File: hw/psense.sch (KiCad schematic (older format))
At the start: 8 parts

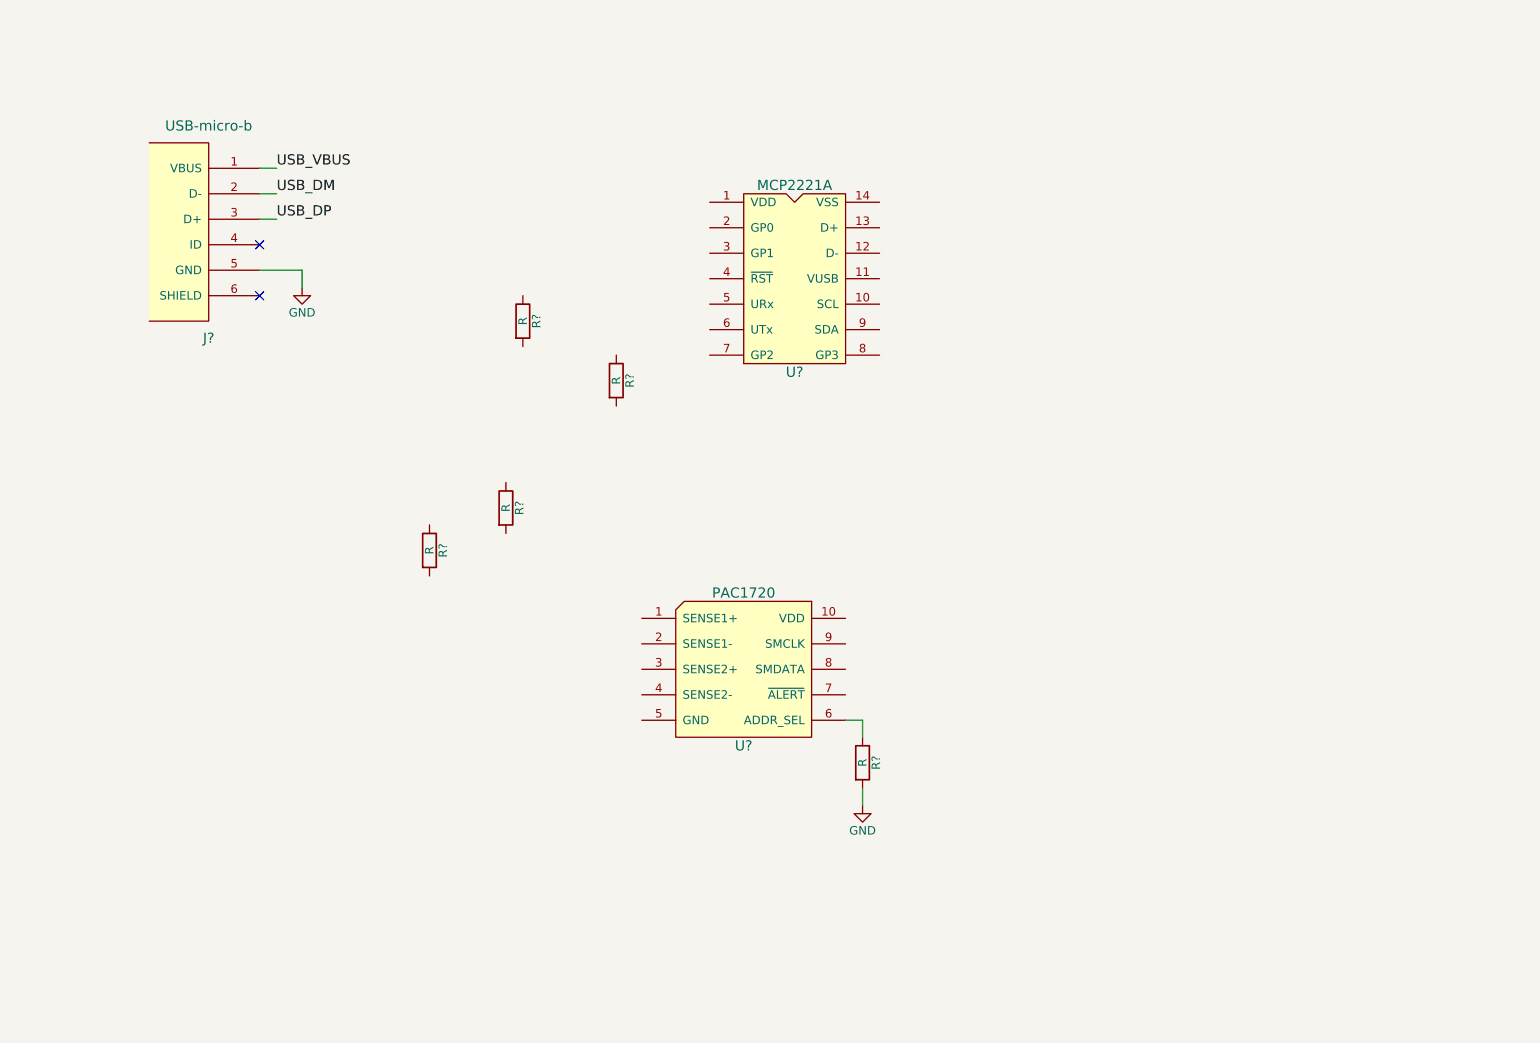
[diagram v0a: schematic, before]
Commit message: Most of schematic done
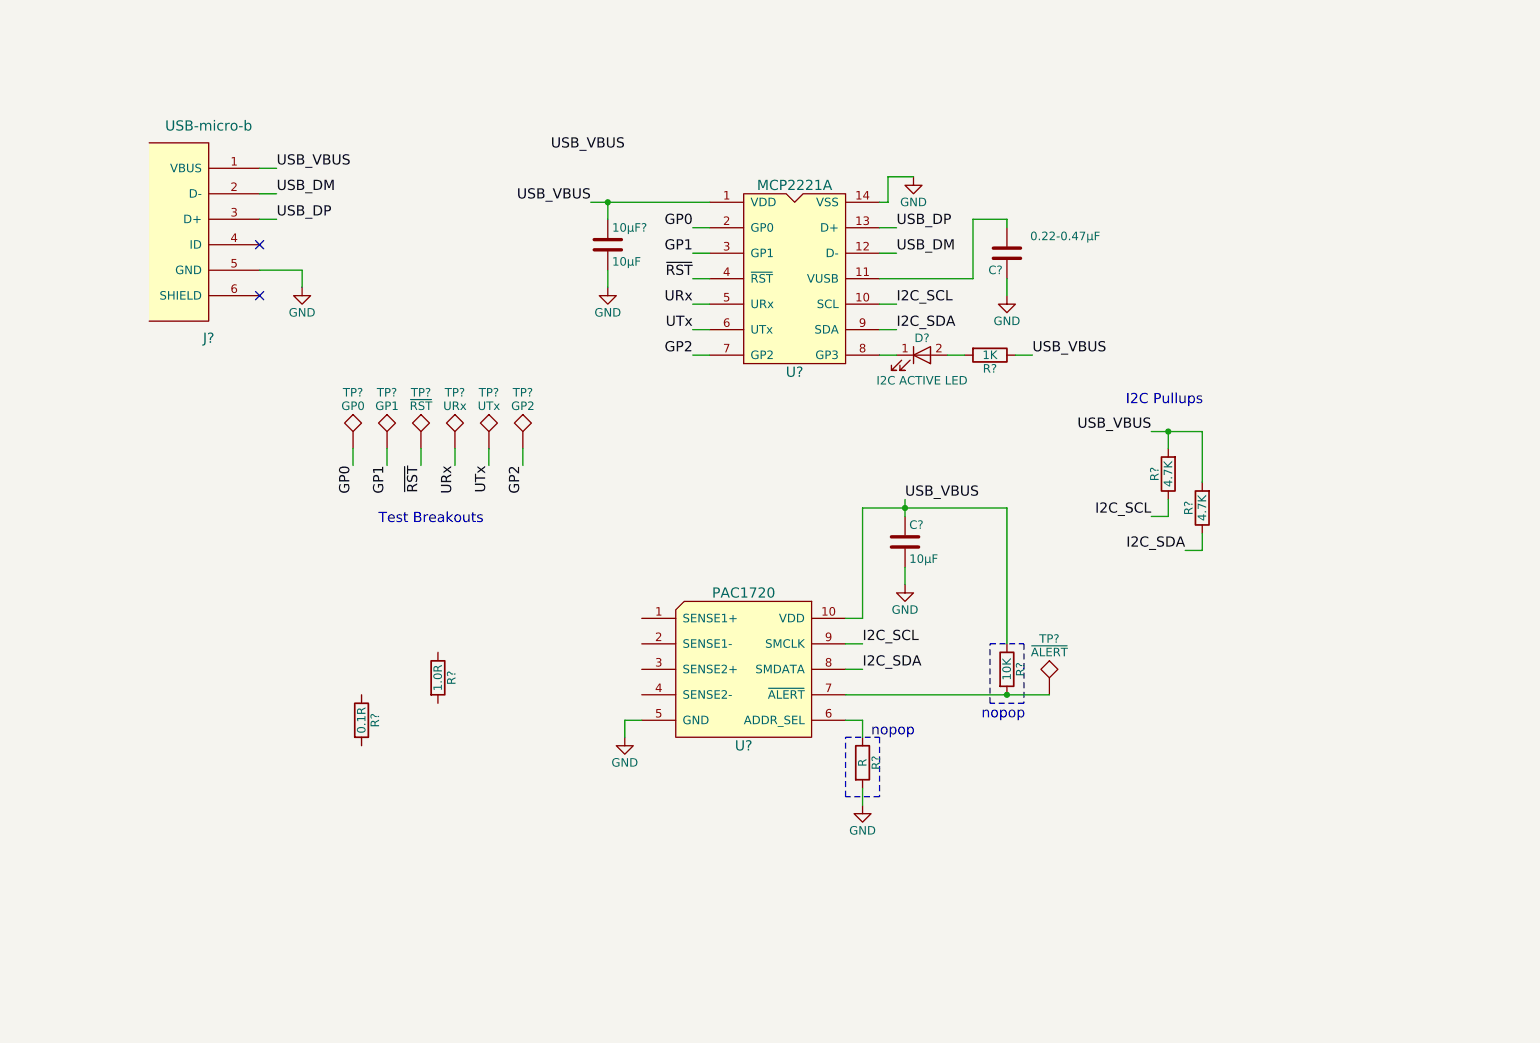
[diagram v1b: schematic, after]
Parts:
- removed R? (x2): R, symbol R
- added 10µF?, C?: 10µF, symbol C
- added C?: 0.22-0.47µF, symbol C
- added D?: I2C ACTIVE LED, symbol LED
- added R?: 10K, symbol R
- added R?: 1K, symbol R
- added R? (x2): 4.7K, symbol R
- added TP?: ~ALERT, symbol TEST
- added TP?: GP2, symbol TEST
- added TP?: URx, symbol TEST
- added TP?: UTx, symbol TEST
- added TP?: ~RST, symbol TEST
- added TP?: GP1, symbol TEST
- added TP?: GP0, symbol TEST
- R?: value R -> 0.1R
- R?: value R -> 1.0R
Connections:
- net GND: now also U?.14 (VSS), U?.5 (GND), 10µF?.2, C?.1, C?.2
- net USB_DM: now also U?.12 (D-)
- net USB_DP: now also U?.13 (D+)
- net USB_VBUS: now also U?.1 (VDD), U?.10 (VDD), 10µF?.1, C?.1, R?.1, R?.1, R?.2, R?.2
- net at U?.7 (~ALERT): now also R?.2, TP?.1
- net I2C_SDA: now reaches U?.8 (SMDATA)
- net I2C_SDA: now also U?.9 (SDA), R?.1
- net I2C_SCL: now reaches U?.9 (SMCLK)
- net I2C_SCL: now also U?.10 (SCL), R?.1
- net at U?.11 (VUSB): now also C?.2
- net GP0: now reaches U?.2 (GP0)
- net GP0: now also TP?.1
- net GP1: now reaches U?.3 (GP1)
- net GP1: now also TP?.1
- net ~RST: now reaches U?.4 (~RST)
- net ~RST: now also TP?.1
- net URx: now reaches U?.5 (URx)
- net URx: now also TP?.1
- net UTx: now reaches U?.6 (UTx)
- net UTx: now also TP?.1
- net GP2: now reaches U?.7 (GP2)
- net GP2: now also TP?.1
- net at U?.8 (GP3): now also D?.1 (K)
- new net: D?.2 (A), R?.2
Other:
- note added: "I2C Pullups"
- note added: "Test Breakouts"
- note added: "nopop"
- moved on the sheet: R?

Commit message: Finish schematic
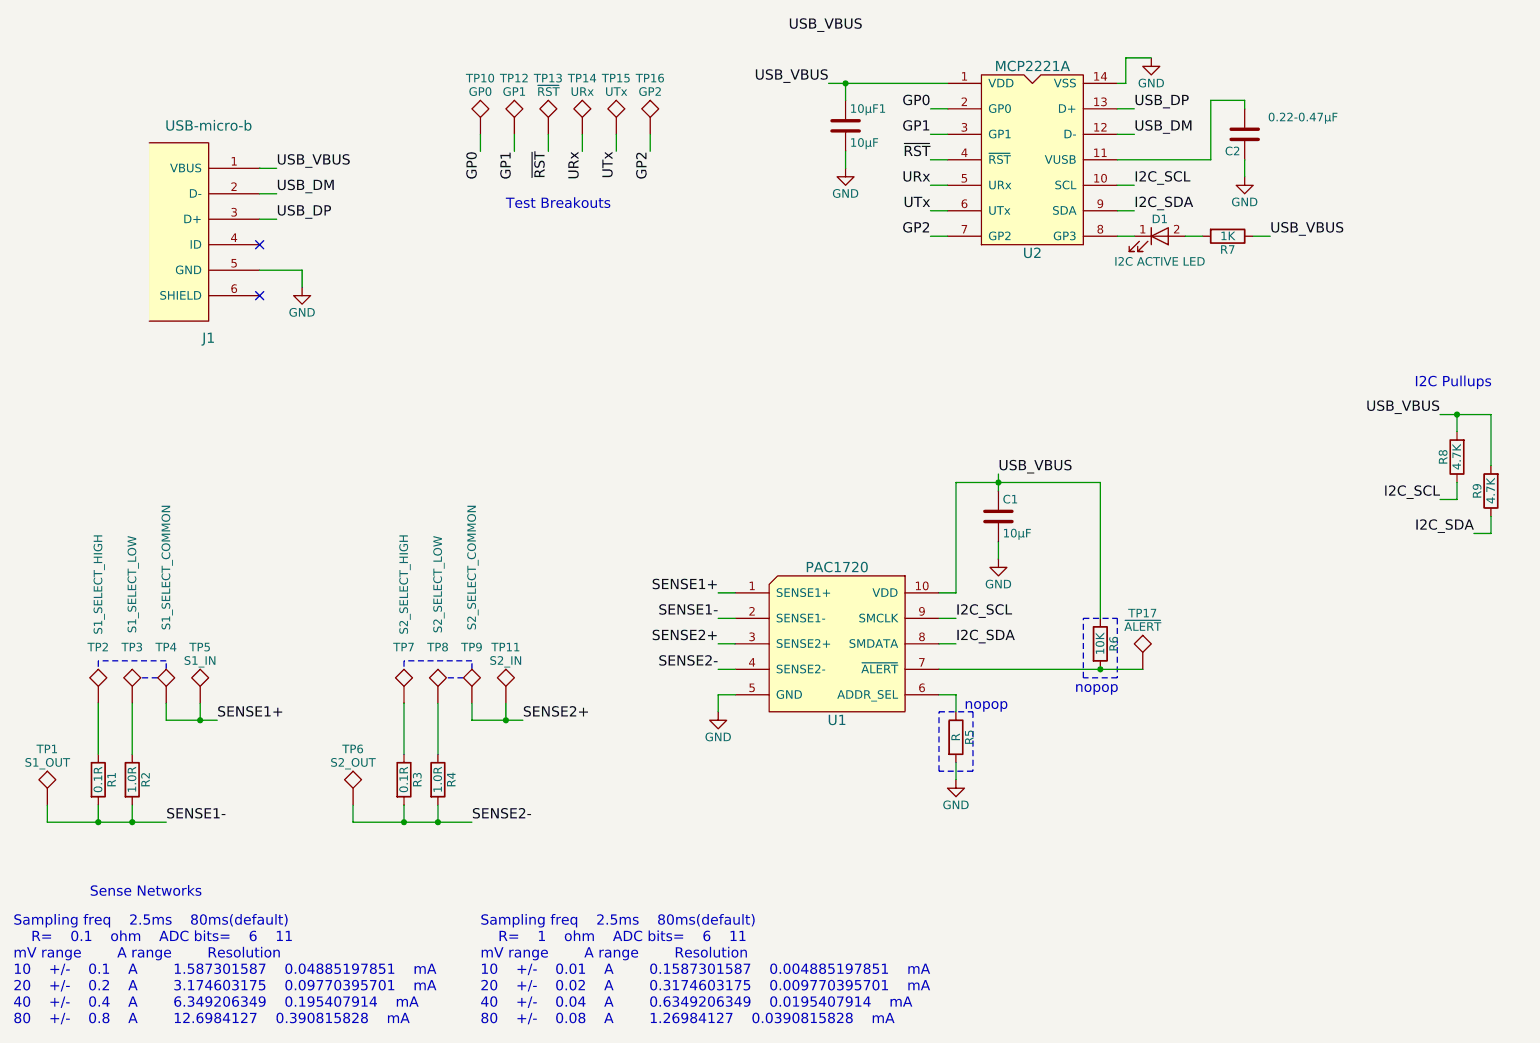
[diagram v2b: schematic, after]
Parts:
- added R3: 0.1R, symbol R
- added R4: 1.0R, symbol R
- added TP1: S1_OUT, symbol TEST
- added TP11: S2_IN, symbol TEST
- added TP2: S1_SELECT_HIGH, symbol TEST
- added TP3: S1_SELECT_LOW, symbol TEST
- added TP4: S1_SELECT_COMMON, symbol TEST
- added TP5: S1_IN, symbol TEST
- added TP6: S2_OUT, symbol TEST
- added TP7: S2_SELECT_HIGH, symbol TEST
- added TP8: S2_SELECT_LOW, symbol TEST
- added TP9: S2_SELECT_COMMON, symbol TEST
- gave numbers to parts that had none: 21
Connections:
- net SENSE1+: now reaches U1.1 (SENSE1+)
- net SENSE1+: now also TP4.1, TP5.1
- net SENSE1-: now reaches U1.2 (SENSE1-)
- net SENSE1-: now also R1.2, R2.2, TP1.1
- net SENSE2+: now reaches U1.3 (SENSE2+)
- net SENSE2+: now also TP11.1, TP9.1
- net SENSE2-: now reaches U1.4 (SENSE2-)
- net SENSE2-: now also R3.2, R4.2, TP6.1
- net at R1.1: now also TP2.1
- net at R2.1: now also TP3.1
- new net: R3.1, TP7.1
- new net: R4.1, TP8.1
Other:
- note added: "Sampling freq 2.5ms 80ms(default) \n R= 0.1 ohm ADC bits= 6 11 \nmV range A range Resolution \n10 +/- 0.1 A 1.587301587 0.04885197851 mA\n20 +/- 0.2 A 3.174603175 0.09770395701 mA\n40 +/- 0.4 A 6.349206349 0.195407914 mA\n80 +/- 0.8 A 12.6984127 0.390815828 mA"
- note added: "Sampling freq 2.5ms 80ms(default) \n R= 1 ohm ADC bits= 6 11 \nmV range A range Resolution \n10 +/- 0.01 A 0.1587301587 0.004885197851 mA\n20 +/- 0.02 A 0.3174603175 0.009770395701 mA\n40 +/- 0.04 A 0.6349206349 0.0195407914 mA\n80 +/- 0.08 A 1.26984127 0.0390815828 mA"
- note added: "Sense Networks"
- moved on the sheet: 10µF1, C1, C2, D1, R1, R2, R5, R6, R7, R8, R9, TP10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
